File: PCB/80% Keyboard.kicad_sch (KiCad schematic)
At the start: 198 parts, among them J1 USB_C_Receptacle_USB2.0_16P, SW1 Esc, SW10 A, SW102 Right, SW11 Z, SW12 Win, SW13 F2, SW14 2, SW15 W, SW16 S, SW17 X, SW18 Alt, SW19 F3, SW2 Tilde ~, SW20 3, SW21 E, SW22 D, SW23 C, SW24 RotaryEncoder, SW25 F4, SW26 4, SW27 R, SW28 F, SW29 V, SW3 Tab, SW30 SW_BOOT, SW31 F5, SW32 5, SW33 T, SW34 G, SW35 B, SW36 Space, SW37 F6, SW38 6, SW39 Y, SW4 CapsLock, SW40 H, SW41 N, SW42 SW_RESET, SW43 F7, SW44 7, SW45 U, SW46 J, SW47 M, SW49 F8, SW5 Shift, SW50 8, SW51 I, SW52 K, SW53 Comma, SW54 R_Alt, SW55 F9, SW56 9, SW57 O, SW58 L, SW59 Full Stop, SW6 Ctrl, SW60 R_Win, SW61 F10, SW62 0, SW63 P, SW64 Semicolon, SW65 F Slash, SW66 Fn, SW67 F11, SW68 Minus -, SW69 [, SW7 F1, SW70 Apostrophe, SW71 R_Shift, SW72 R_Ctrl, SW73 F12, SW74 Plus +, SW75 ], SW76 Enter, SW8 1, SW80 Backspace, SW81 B Slash, SW85 PrtSc, SW86 Insert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

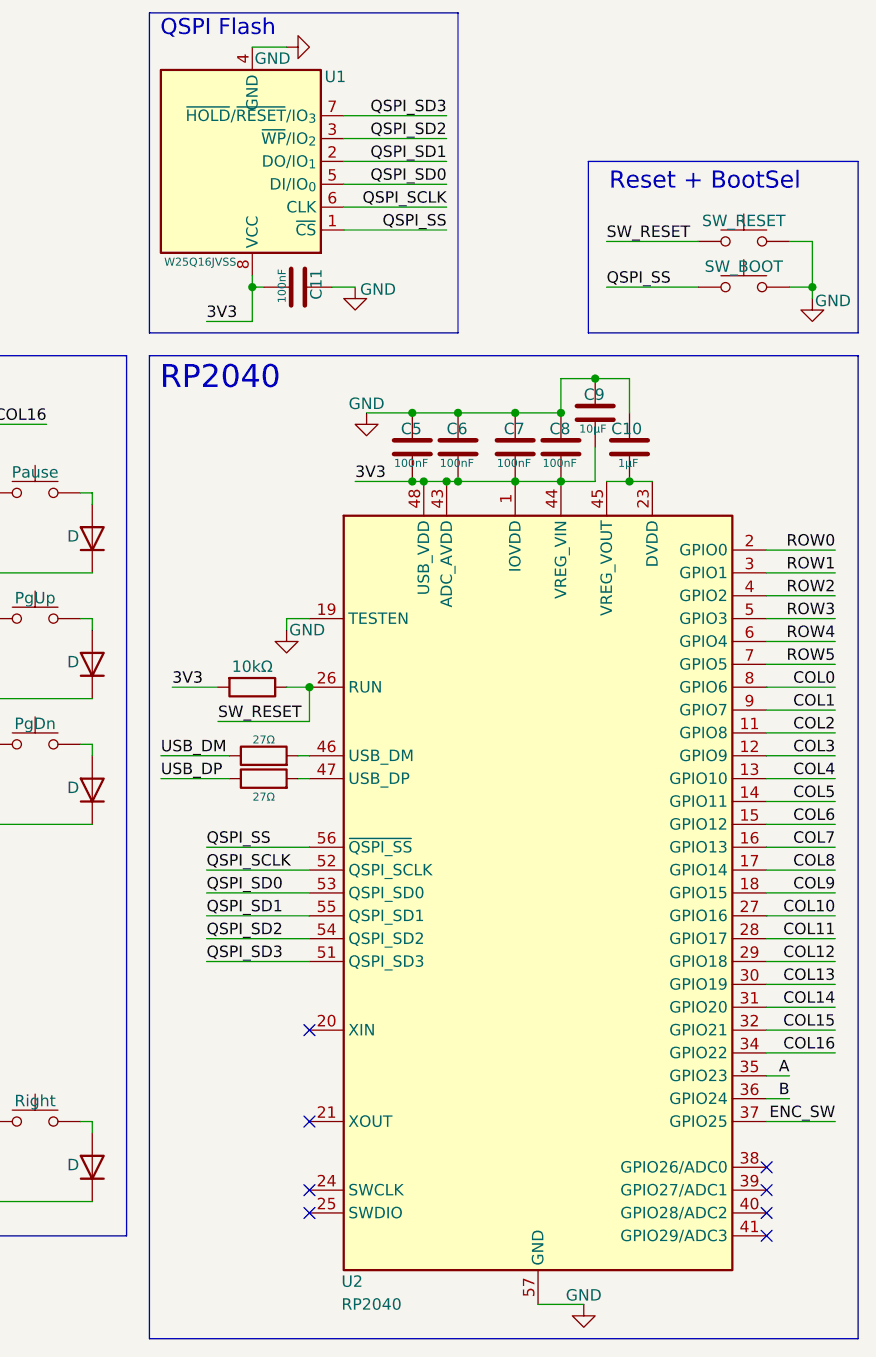
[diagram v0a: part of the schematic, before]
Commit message: Added Crystal
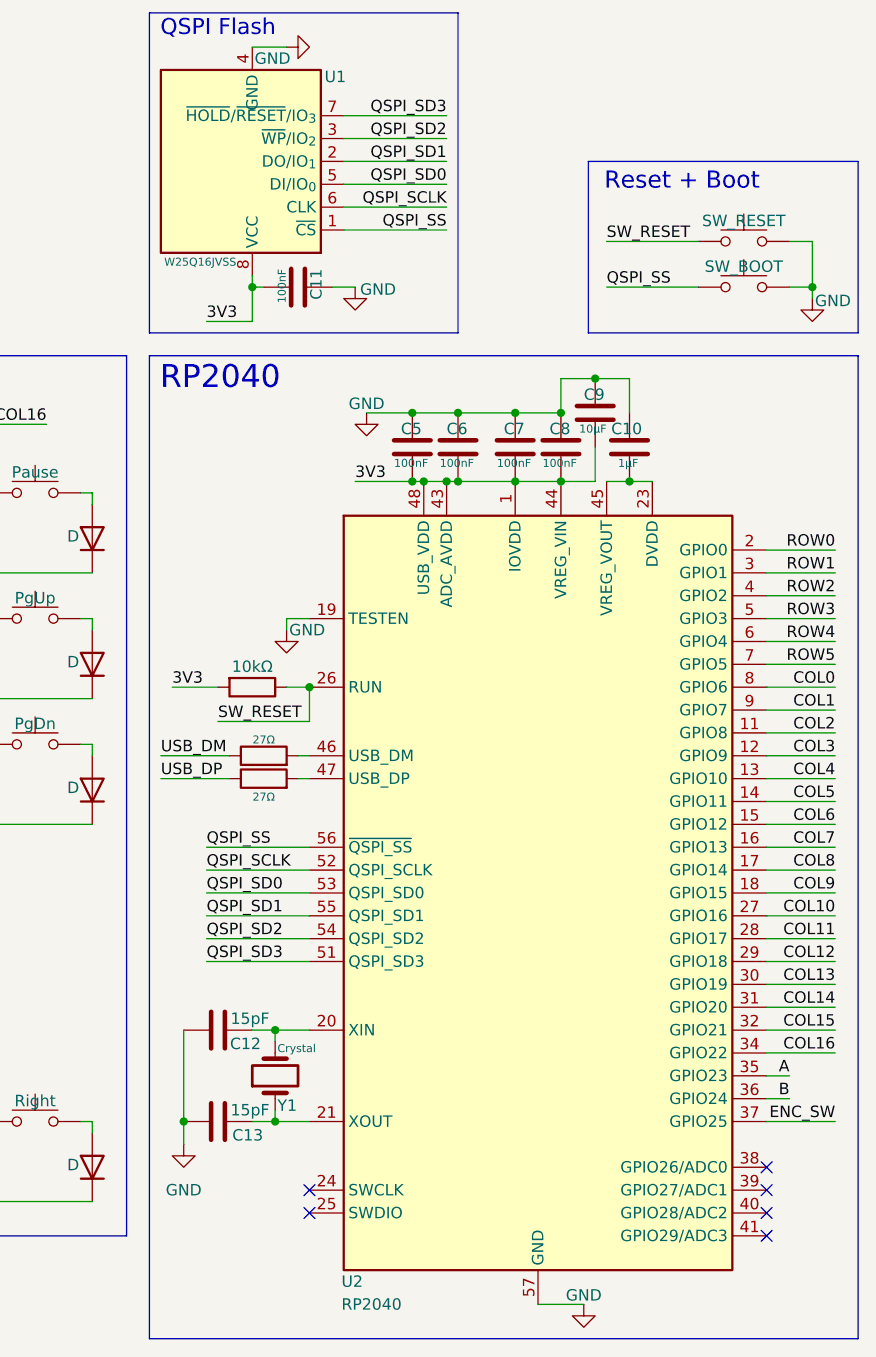
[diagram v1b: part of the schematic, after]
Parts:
- added C12, C13: 15pF, Capacitor_SMD:C_0402_1005Metric_Pad0.74x0.62mm_HandSolder, symbol Device:C
- added Y1: Crystal, Crystal:Crystal_SMD_3225-4Pin_3.2x2.5mm_HandSoldering, symbol Device:Crystal
- C1, C10, C11, C2, C3, C4, C5, C6, C7, C8, C9: footprint Capacitor_SMD:C_0402_1005Metric -> Capacitor_SMD:C_0402_1005Metric_Pad0.74x0.62mm_HandSolder
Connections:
- net GND: now also C12.1, C13.1
- net at U2.20 (XIN): now also C12.2, Y1.2
- net at U2.21 (XOUT): now also C13.2, Y1.1
- no-connect marks 10 -> 8
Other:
- note added: "Reset + Boot"
- note removed: "Reset + BootSel"

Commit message: Entire PCB + Updated Journal.MD
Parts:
- J1: footprint Connector_USB:USB_C_Receptacle_GCT_USB4135-GF-A_6P_TopMnt_Horizontal -> Connector_USB:USB_C_Receptacle_GCT_USB4105-xx-A_16P_TopMnt_Horizontal
- SW24: footprint Rotary_Encoder:RotaryEncoder_Alps_EC11E_Vertical_H20mm -> Rotary_Encoder:RotaryEncoder_Alps_EC11E-Switch_Vertical_H20mm
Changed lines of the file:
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@@
 			)
 		)
-		(property "Footprint" "Rotary_Encoder:RotaryEncoder_Alps_EC11E_Vertical_H20mm"
+		(property "Footprint" "Rotary_Encoder:RotaryEncoder_Alps_EC11E-Switch_Vertical_H20mm"
 			(at 252.73 86.106 0)
 			(effects
@@
 			)
 		)
-		(property "Footprint" "Connector_USB:USB_C_Receptacle_GCT_USB4135-GF-A_6P_TopMnt_Horizontal"
+		(property "Footprint" "Connector_USB:USB_C_Receptacle_GCT_USB4105-xx-A_16P_TopMnt_Horizontal"
 			(at 43.18 69.85 0)
 			(effects

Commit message: Artwork + Name + Journal
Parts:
- added H1, H2, H3, H4, H5, H6: M2, MountingHole:MountingHole_2.2mm_M2, symbol Mechanical:MountingHole
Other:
- note added: "Moutning Screws"
- moved on the sheet: C1, C2, C3, C4, U3, U4

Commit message: Bom Stuff
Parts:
- removed H1, H2, H3, H4, H5, H6: M2, MountingHole:MountingHole_2.2mm_M2, symbol Mechanical:MountingHole
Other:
- note removed: "Moutning Screws"
